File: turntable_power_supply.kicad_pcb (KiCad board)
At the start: 2 copper layers, 65 x 56 mm, 34 parts, among them IC15 171032401, IC235 171032401, IC5 171032401, X15 694106301002, X235 694106301002, X24 694106301002, X5 PRT-21570

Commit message: Add missing trace
Signed-off-by: Marc 'risson' Schmitt <marc.schmitt@risson.space>
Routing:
- net VSS: track 3.25 -> 14.7 mm
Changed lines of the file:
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@@
 			(layer "F.Fab")
 		)
-		(fp_text user "1"
-			(at 4.2 0.7 180)
-			(layer "F.SilkS")
-			(effects
-				(font
-					(size 1 1)
-					(thickness 0.15)
-				)
-			)
-		)
-		(fp_text user "2"
-			(at -1.7 0.6 180)
-			(layer "F.SilkS")
-			(effects
-				(font
-					(size 1 1)
-					(thickness 0.15)
-				)
-			)
-		)
-		(fp_text user "3"
-			(at 2.3 3.5 180)
-			(layer "F.SilkS")
-			(effects
-				(font
-					(size 1 1)
-					(thickness 0.15)
-				)
-			)
-		)
-		(fp_text user "PCB Cutout Area"
-			(at 0.1 0 180)
-			(layer "Edge.Cuts")
-			(effects
-				(font
-					(size 0.2 0.2)
-					(thickness 0.15)
-				)
-			)
-		)
-		(fp_text user "PCB Cutout Area"
-			(at 2.9 5 180)
-			(layer "Edge.Cuts")
-			(effects
-				(font
-					(size 0.2 0.2)
-					(thickness 0.15)
-				)
-			)
-		)
-		(fp_text user "PCB Cutout Area"
-			(at 5.9 0 180)
-			(layer "Edge.Cuts")
-			(effects
-				(font
-					(size 0.2 0.2)
-					(thickness 0.15)
-				)
-			)
-		)
 		(pad "1" thru_hole circle
 			(at 5.8 0 180)
@@
 			(layer "F.Fab")
 		)
-		(fp_text user "3"
-			(at 2.3 3.5 180)
-			(layer "F.SilkS")
-			(effects
-				(font
-					(size 1 1)
-					(thickness 0.15)
-				)
-			)
-		)
-		(fp_text user "1"
-			(at 4.2 0.7 180)
-			(layer "F.SilkS")
-			(effects
-				(font
-					(size 1 1)
-					(thickness 0.15)
-				)
-			)
-		)
-		(fp_text user "2"
-			(at -1.7 0.6 180)
-			(layer "F.SilkS")
-			(effects
-				(font
-					(size 1 1)
-					(thickness 0.15)
-				)
-			)
-		)
-		(fp_text user "PCB Cutout Area"
-			(at 2.9 5 180)
-			(layer "Edge.Cuts")
-			(effects
-				(font
-					(size 0.2 0.2)
-					(thickness 0.15)
-				)
-			)
-		)
-		(fp_text user "PCB Cutout Area"
-			(at 0.1 0 180)
-			(layer "Edge.Cuts")
-			(effects
-				(font
-					(size 0.2 0.2)
-					(thickness 0.15)
-				)
-			)
-		)
-		(fp_text user "PCB Cutout Area"
-			(at 5.9 0 180)
-			(layer "Edge.Cuts")
-			(effects
-				(font
-					(size 0.2 0.2)
-					(thickness 0.15)
-				)
-			)
-		)
 		(pad "1" thru_hole circle
 			(at 5.8 0 180)
@@
 			(layer "F.Fab")
 		)
-		(fp_text user "2"
-			(at -1.7 0.6 180)
-			(layer "F.SilkS")
-			(effects
-				(font
-					(size 1 1)
-					(thickness 0.15)
-				)
-			)
-		)
-		(fp_text user "1"
-			(at 4.2 0.7 180)
-			(layer "F.SilkS")
-			(effects
-				(font
-					(size 1 1)
-					(thickness 0.15)
-				)
-			)
-		)
-		(fp_text user "3"
-			(at 2.3 3.5 180)
-			(layer "F.SilkS")
-			(effects
-				(font
-					(size 1 1)
-					(thickness 0.15)
-				)
-			)
-		)
-		(fp_text user "PCB Cutout Area"
-			(at 0.1 0 180)
-			(layer "Edge.Cuts")
-			(effects
-				(font
-					(size 0.2 0.2)
-					(thickness 0.15)
-				)
-			)
-		)
-		(fp_text user "PCB Cutout Area"
-			(at 5.9 0 180)
-			(layer "Edge.Cuts")
-			(effects
-				(font
-					(size 0.2 0.2)
-					(thickness 0.15)
-				)
-			)
-		)
-		(fp_text user "PCB Cutout Area"
-			(at 2.9 5 180)
-			(layer "Edge.Cuts")
-			(effects
-				(font
-					(size 0.2 0.2)
-					(thickness 0.15)
-				)
-			)
-		)
 		(pad "1" thru_hole circle
 			(at 5.8 0 180)
@@
 	)
 	(segment
+		(start 170.7 74.85)
+		(end 170.15 74.3)
+		(width 0.9)
+		(layer "F.Cu")
+		(net 2)
+	)
+	(segment
 		(start 166.9 74.3)
 		(end 170.15 74.3)
 		(width 0.9)
 		(layer "F.Cu")
+		(net 2)
+	)
+	(segment
+		(start 170.7 85.5)
+		(end 170.7 74.85)
+		(width 0.9)
+		(layer "F.Cu")

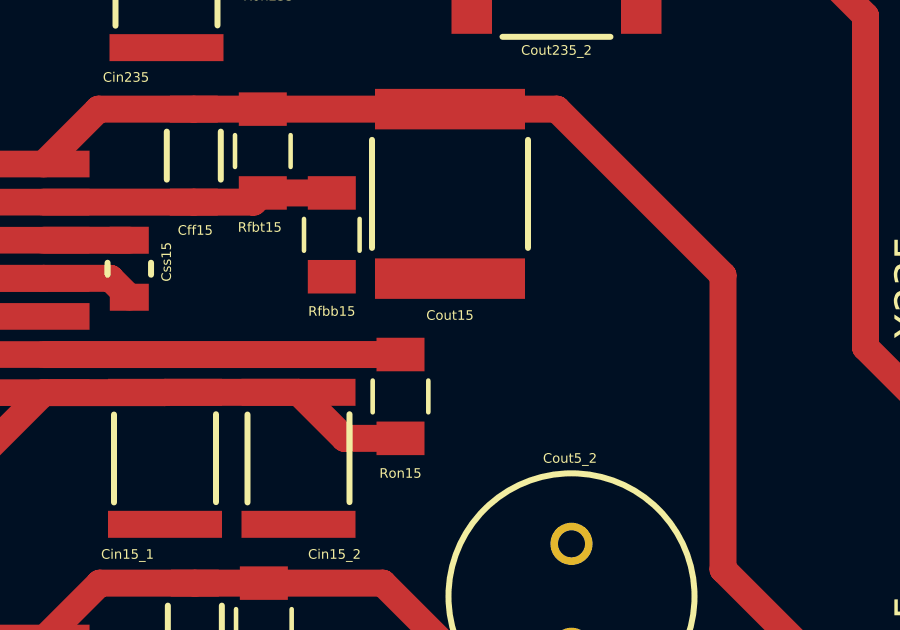
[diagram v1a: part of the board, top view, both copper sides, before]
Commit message: Fix Cout_15 footprint
Signed-off-by: Marc 'risson' Schmitt <marc.schmitt@risson.space>
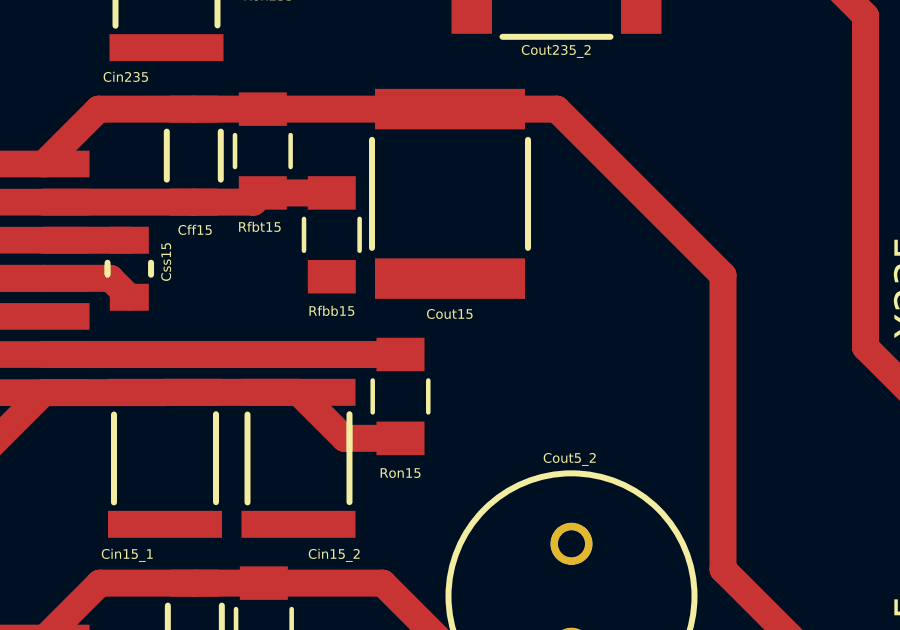
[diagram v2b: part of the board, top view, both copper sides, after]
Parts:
- Cout15: footprint 885012214006:885012214006 -> 885012214005:885012214005
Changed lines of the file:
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@@
 		)
 		(property "Value" "10uF"
-			(at 0 3.492 360)
+			(at 0 3.492 0)
 			(layer "F.Fab")
 			(hide yes)
@@
 		)
 		(property "Footprint" "885012214006:885012214006"
-			(at 0 0 360)
+			(at 0 0 0)
 			(layer "F.Fab")
 			(hide yes)
@@
 		)
 		(property "Datasheet" ""
-			(at 0 0 360)
+			(at 0 0 0)
 			(layer "F.Fab")
 			(hide yes)
@@
 		)
 		(property "Description" ""
-			(at 0 0 360)
+			(at 0 0 0)
 			(layer "F.Fab")
 			(hide yes)
@@
 		)
 		(property "Value" "10uF"
-			(at 0 3.492 360)
+			(at 0 3.492 0)
 			(layer "F.Fab")
 			(hide yes)
@@
 		)
 		(property "Footprint" "885012214006:885012214006"
-			(at 0 0 360)
+			(at 0 0 0)
 			(layer "F.Fab")
 			(hide yes)
@@
 		)
 		(property "Datasheet" ""
-			(at 0 0 360)
+			(at 0 0 0)
 			(layer "F.Fab")
 			(hide yes)
@@
 		)
 		(property "Description" ""
-			(at 0 0 360)
+			(at 0 0 0)
 			(layer "F.Fab")
 			(hide yes)
@@
 		(descr "<B>WCAP-PT5H</B><BR>  Aluminium Polymer Capacitors ,8x11.5x3.5x0.6(DiameterXLengthXPinXØ Pin)")
 		(property "Reference" "Cout5_2"
-			(at -4.6 0.05 360)
+			(at -4.6 0.05 0)
 			(layer "F.SilkS")
 			(effects
@@
 		)
 	)
-	(footprint "885012214006:885012214006"
+	(footprint "885012214005:885012214005"
 		(layer "F.Cu")
 		(at 153.25 90.185 -90)
 		(descr "<b>WCAP-CSGP MLCCs 1812</b><br>4.5X3.2X2.5(LXWXH)")
 		(property "Reference" "Cout15"
-			(at 4.05 0 360)
+			(at 4.015 0 0)
 			(layer "F.SilkS")
 			(effects
@@
 		)
 		(property "Value" "10uF"
-			(at 0 3.492 90)
+			(at 0 3.492 -90)
 			(layer "F.Fab")
 			(hide yes)
@@
 			)
 		)
-		(property "Footprint" "885012214006:885012214006"
-			(at 0 0 90)
+		(property "Footprint" "885012214005:885012214005"
+			(at 0 0 -90)
 			(layer "F.Fab")
 			(hide yes)
@@
 		)
 		(property "Datasheet" ""
-			(at 0 0 90)
+			(at 0 0 -90)
 			(layer "F.Fab")
 			(hide yes)
@@
 		)
 		(property "Description" ""
-			(at 0 0 90)
+			(at 0 0 -90)
 			(layer "F.Fab")
 			(hide yes)
@@
 			(solder_mask_margin 0.102)
 		)
-		(model "${KIPRJMOD}/libraries/885012214006/885012214006.stp"
-			(offset
-				(xyz 0 0 1.4)
-			)
-			(scale
-				(xyz 1 1 1)
-			)
-			(rotate
-				(xyz 0 0 0)
-			)
-		)
 	)
